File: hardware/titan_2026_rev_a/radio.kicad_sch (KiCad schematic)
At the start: 9 parts, among them J12 BWSMA-KWE-Z001, U11 ATGM336H-5N31, U12 NRF24L01_Breakout, U13 AT2659S

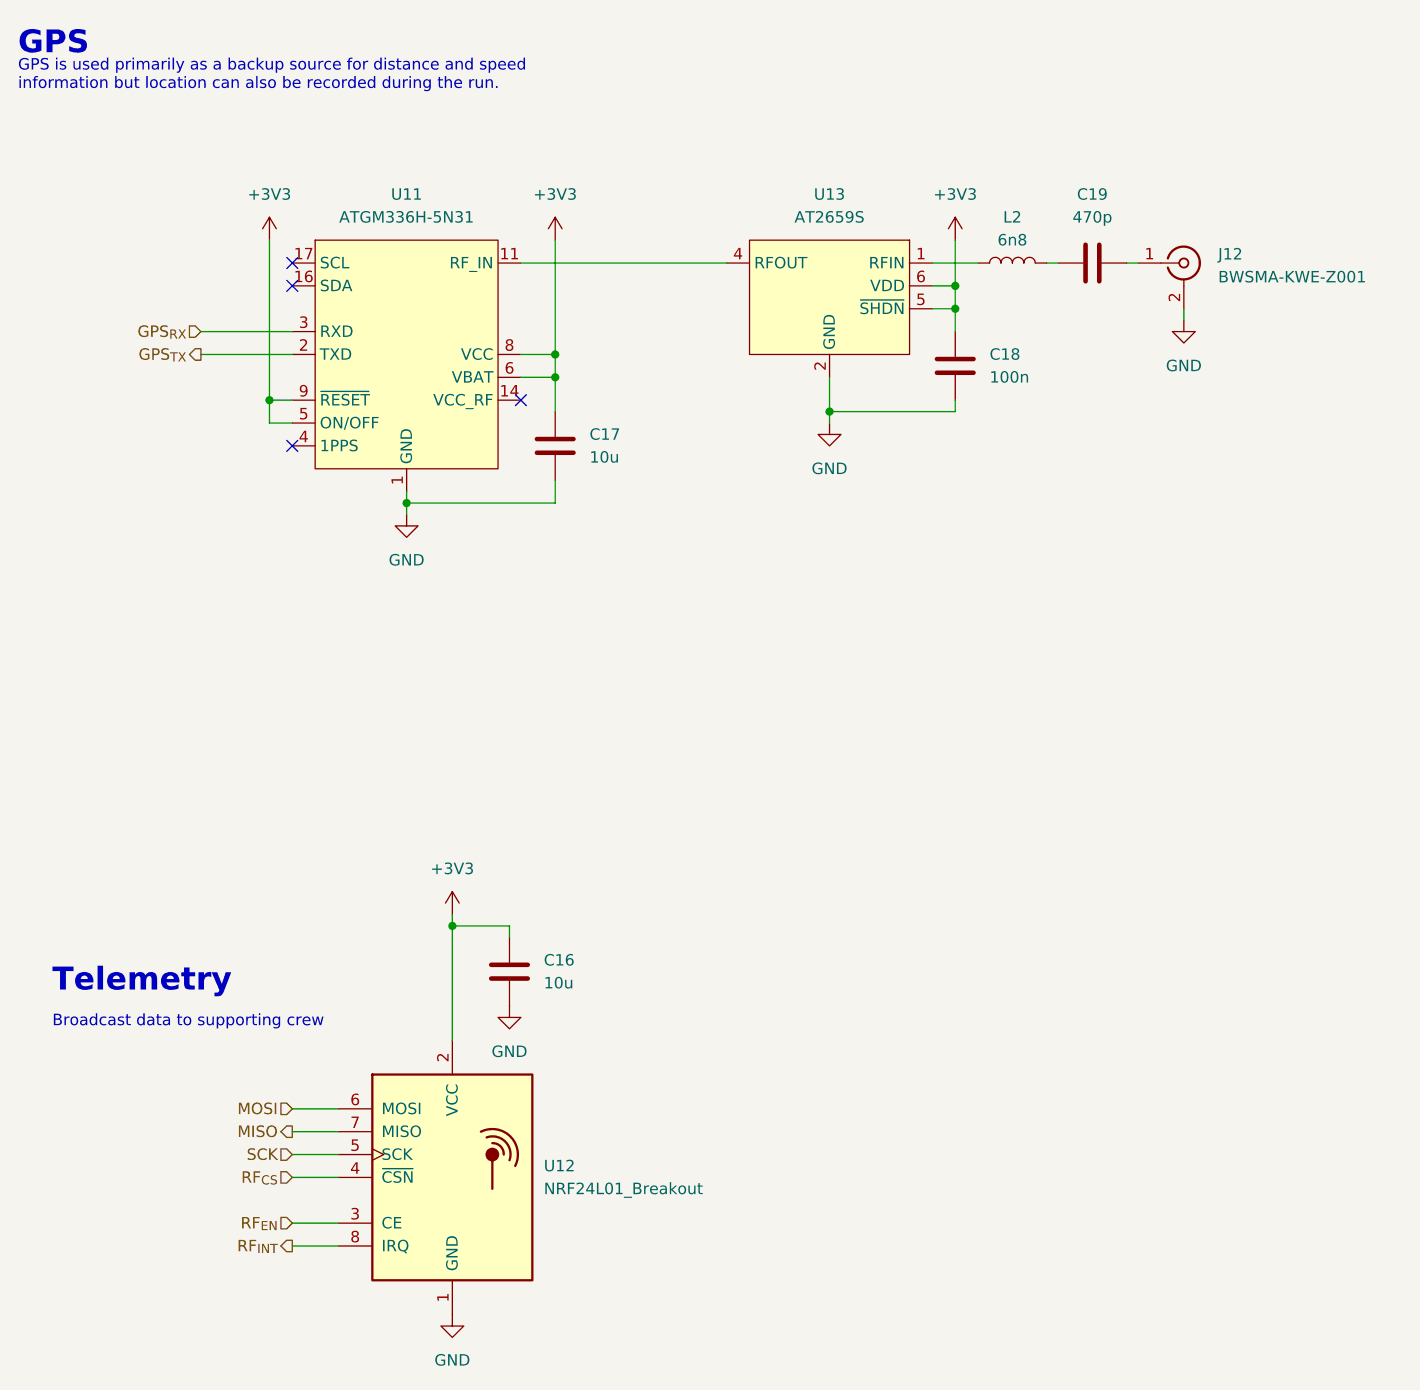
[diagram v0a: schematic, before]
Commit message: Completed schematics for rev A
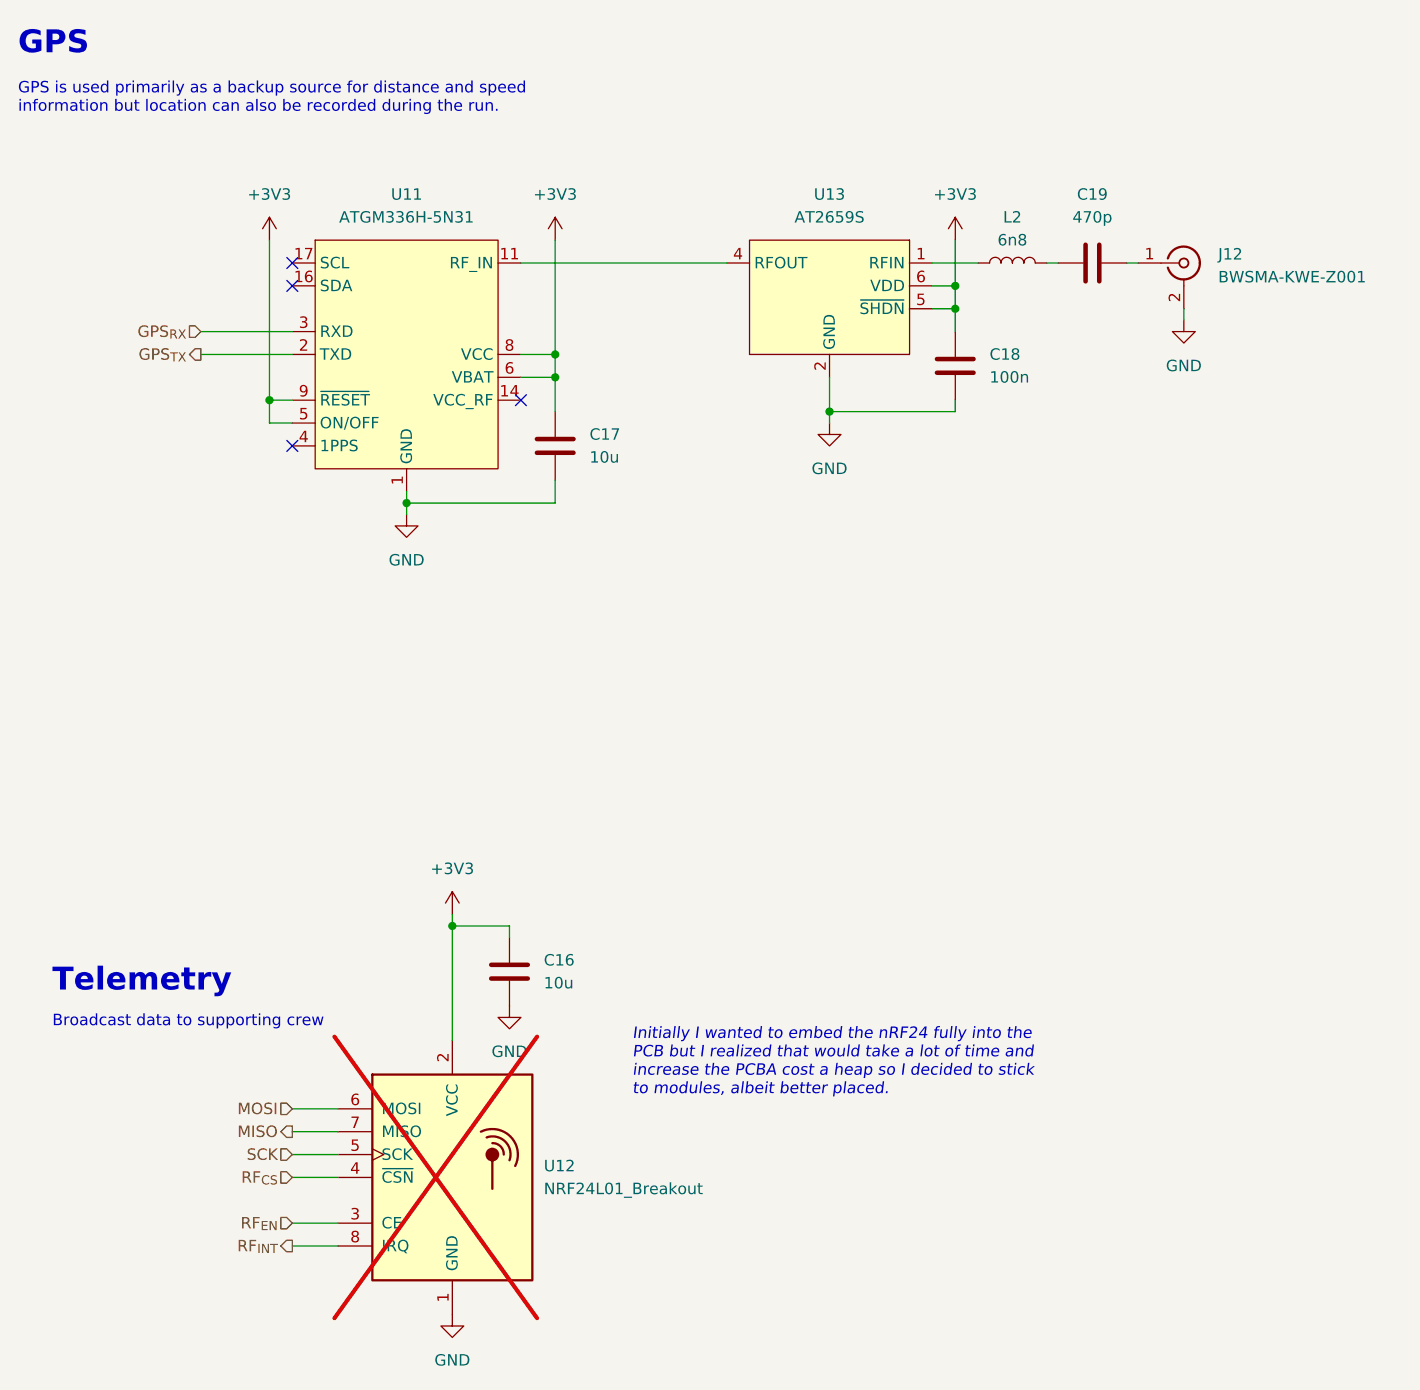
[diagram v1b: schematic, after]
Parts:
- U12: footprint RF_Module:nRF24L01_Breakout -> titan:nRF24L01_PA_LNA_Breakout; now not fitted
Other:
- company: (none) -> Savo Bajic
- title: (none) -> Radio Systems
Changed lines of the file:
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@@
 	(generator "eeschema")
 	(generator_version "10.0")
-	(paper "A4")
+	(paper "USLetter")
+	(title_block
+		(title "Radio Systems")
+		(date "2026-04-22")
+		(rev "A")
+		(company "Savo Bajic")
+		(comment 1 "Radio communications between TITAN and the rest of the team as well as GPS")
+	)
 	(text "Broadcast data to supporting crew"
 		(exclude_from_sim no)
@@
 	(text "GPS is used primarily as a backup source for distance and speed\ninformation but location can also be recorded during the run."
 		(exclude_from_sim no)
-		(at 46.99 36.83 0)
+		(at 46.99 39.37 0)
 		(effects
 			(font
@@
 			)
 			(justify left bottom)
+		)
+	)
+	(text_box "Initially I wanted to embed the nRF24 fully into the PCB but I realized that would take a lot of time and increase the PCBA cost a heap so I decided to stick to modules, albeit better placed."
+		(exclude_from_sim no)
+		(at 114.3 139.7 0)
+		(size 55.88 10.16)
+		(margins 0.9525 0.9525 0.9525 0.9525)
+		(stroke
+			(width -0.0001)
+			(type solid)
+		)
+		(fill
+			(type none)
+		)
+		(effects
+			(font
+				(size 1.27 1.27)
+				(italic yes)
+			)
+			(justify left top)
 		)
 	)
@@
 		(on_board yes)
 		(in_pos_files yes)
-		(dnp no)
+		(dnp yes)
 		(fields_autoplaced yes)
 		(property "Reference" "U12"
@@
 			)
 		)
-		(property "Footprint" "RF_Module:nRF24L01_Breakout"
+		(property "Footprint" "titan:nRF24L01_PA_LNA_Breakout"
 			(at 99.06 142.24 0)
 			(hide yes)
